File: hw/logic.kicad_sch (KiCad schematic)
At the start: 39 parts, among them J6 UART, J7 ESP_PWR, SW2 SW_Push, SW3 SW_Push, U7 BMP280, U8 LSM303C, U9 ESP32-C6-MINI-1/U, Y1 32.768k

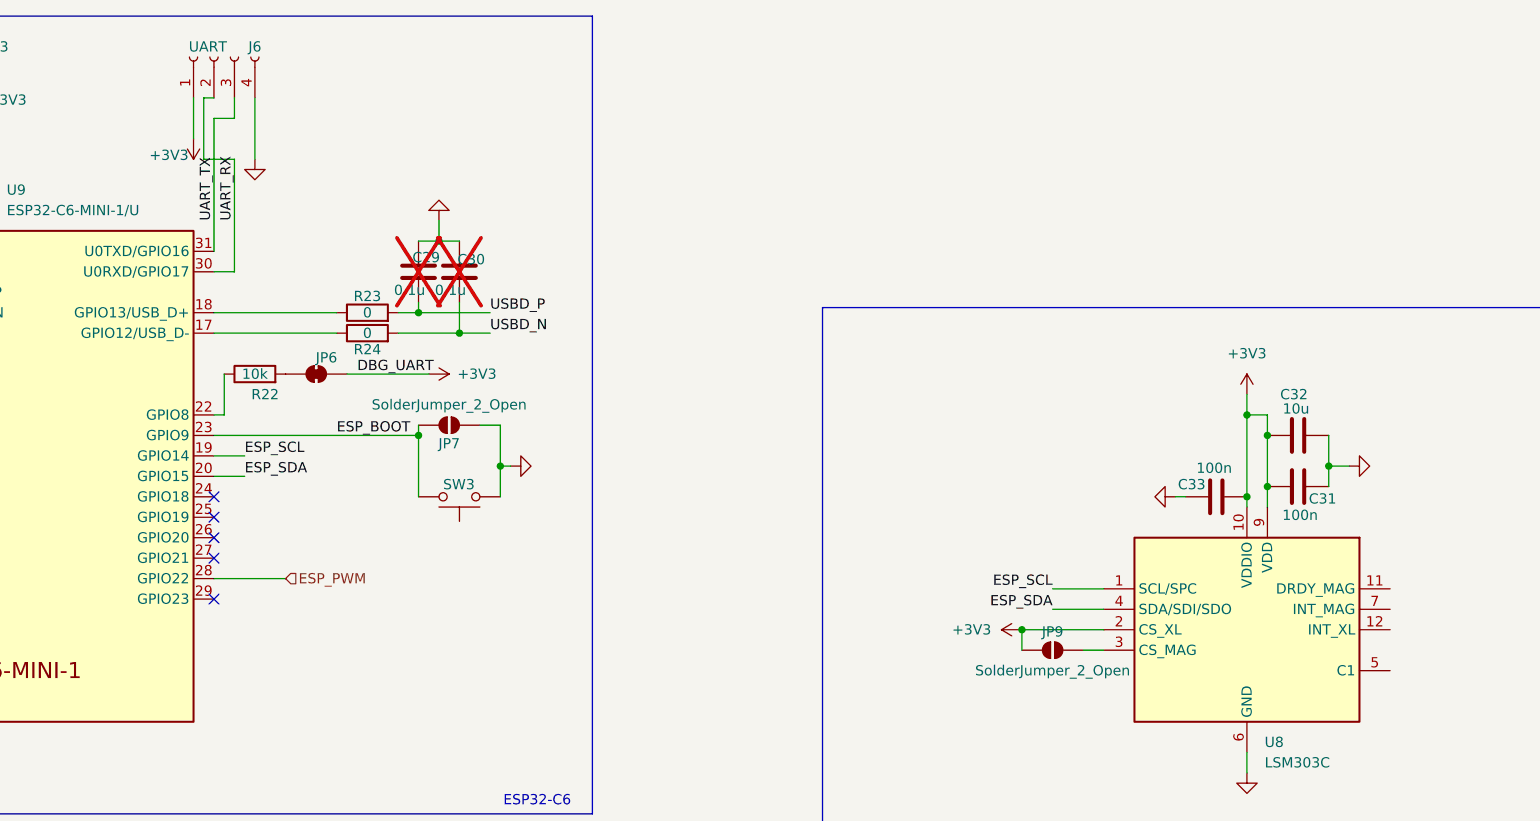
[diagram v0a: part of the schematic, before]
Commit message: Redesign work
I'm going towards a single-sided minimum viable design, so that I only need to place and hotplate one side to  verify function, before adding things like battery and USB by hand.
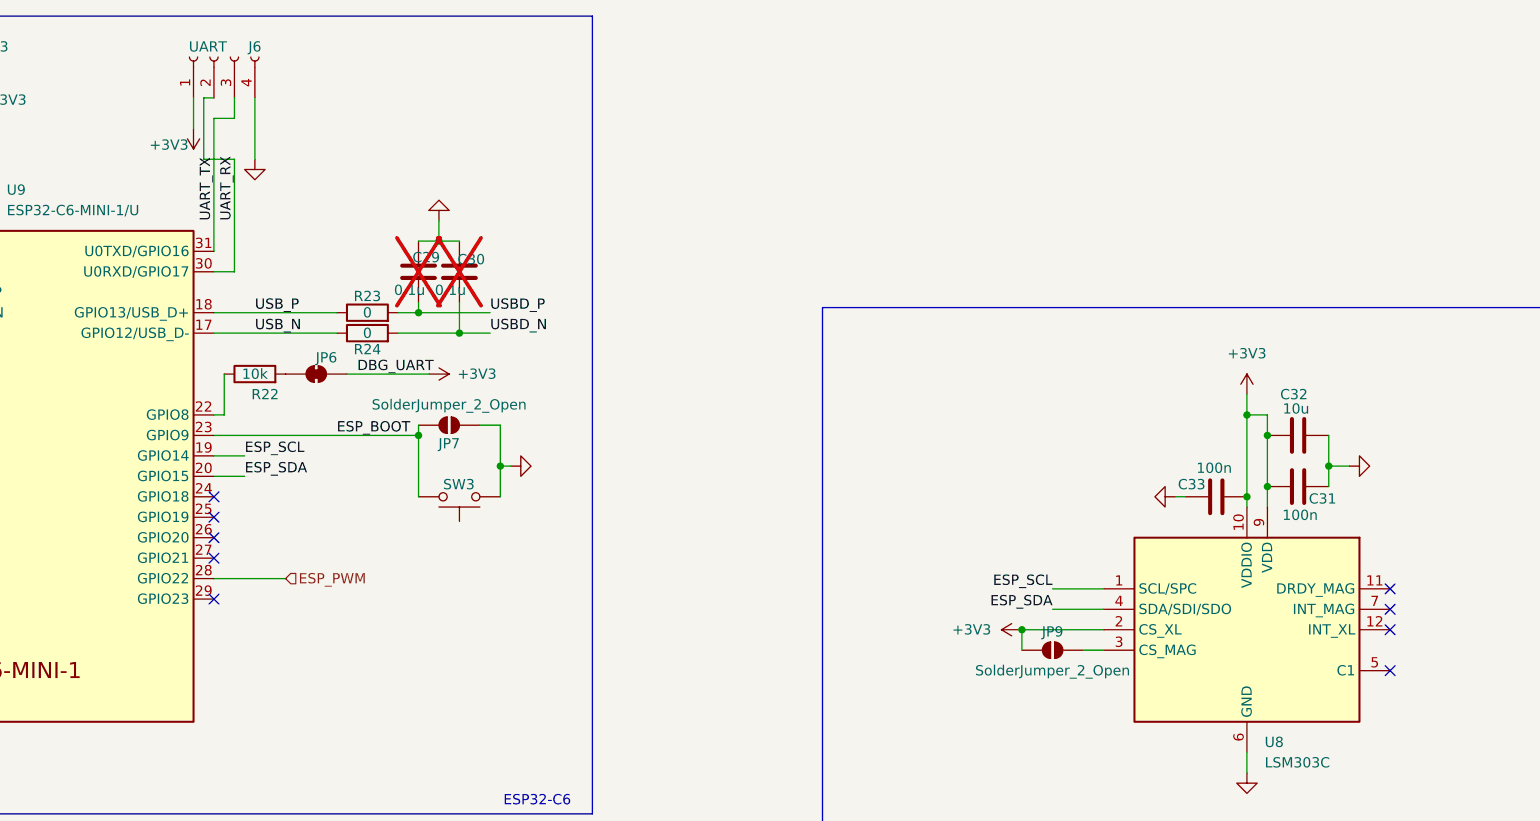
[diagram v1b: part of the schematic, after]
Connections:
- net USB_N: now reaches R24.1, U9.17 (GPIO12/USB_D-)
- net USB_P: now reaches R23.1, U9.18 (GPIO13/USB_D+)
- no-connect marks 6 -> 10
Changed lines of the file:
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@@
 	)
 	(no_connect
+		(at 261.62 93.98)
+	)
+	(no_connect
 		(at 115.57 72.39)
 	)
@@
 	)
 	(no_connect
+		(at 261.62 86.36)
+	)
+	(no_connect
+		(at 261.62 83.82)
+	)
+	(no_connect
+		(at 261.62 88.9)
+	)
+	(no_connect
 		(at 115.57 80.01)
 	)
@@
 	(wire
 		(pts
-			(xy 113.03 22.86) (xy 113.03 27.94)
+			(xy 113.03 22.86) (xy 113.03 26.67)
 		)
 		(stroke
@@
 		)
 	)
+	(label "USB_N"
+		(at 120.65 52.07 0)
+		(effects
+			(font
+				(size 1.27 1.27)
+			)
+			(justify left bottom)
+		)
+	)
 	(label "ESP_SDA"
 		(at 243.84 128.27 90)
@@
 		)
 	)
+	(label "USB_P"
+		(at 120.65 49.53 0)
+		(effects
+			(font
+				(size 1.27 1.27)
+			)
+			(justify left bottom)
+		)
+	)
 	(label "VBAT_MON"
 		(at 43.18 64.77 90)
@@
 		(on_board yes)
 		(dnp no)
-		(fields_autoplaced yes)
 		(property "Reference" "U9"
 			(at 89.8241 34.29 0)
@@
 	(symbol
 		(lib_id "power:+3V3")
-		(at 113.03 27.94 180)
+		(at 113.03 26.67 180)
 		(unit 1)
 		(exclude_from_sim no)
@@
 		(dnp no)
 		(property "Reference" "#PWR39"
-			(at 113.03 24.13 0)
+			(at 113.03 22.86 0)
 			(effects
 				(font
@@
 		)
 		(property "Value" "+3V3"
-			(at 109.982 29.972 0)
+			(at 109.982 28.702 0)
 			(effects
 				(font
@@
 		)
 		(property "Footprint" ""
-			(at 113.03 27.94 0)
+			(at 113.03 26.67 0)
 			(effects
 				(font
@@
 		)
 		(property "Datasheet" ""
-			(at 113.03 27.94 0)
+			(at 113.03 26.67 0)
 			(effects
 				(font
@@
 		)
 		(property "Description" "Power symbol creates a global label with name \"+3V3\""
-			(at 113.03 27.94 0)
+			(at 113.03 26.67 0)
 			(effects
 				(font
